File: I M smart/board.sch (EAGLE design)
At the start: 26 parts, among them IC1 TL072P

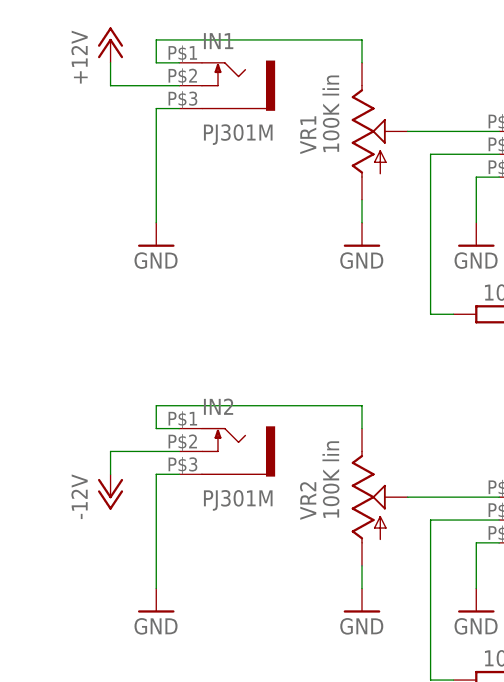
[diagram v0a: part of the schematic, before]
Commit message: Don't connect the power rails directly to output as it shorts the entire case if connected to GND!
Update I M smart to rev0.1. Compatible with panel.
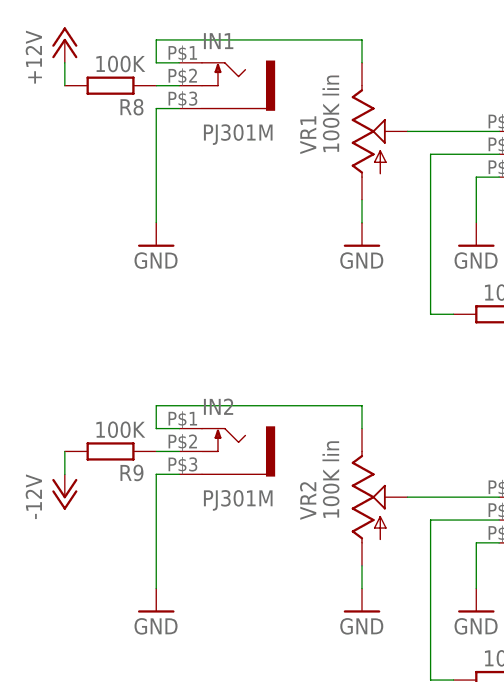
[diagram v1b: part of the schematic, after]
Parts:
- added R8, R9: 100K, rcl:R-EU_0204/5
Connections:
- new net N$11: IN2.3, R9.1
- new net N$12: IN1.3, R8.1
- net +12V: now also R8.2; no longer IN1.3
- net -12V: now also R9.2; no longer IN2.3
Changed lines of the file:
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@@
+<attribute name="OC_FARNELL" value="2329853"/>
+</part>
+<part name="R8" library="rcl" library_urn="urn:adsk.eagle:library:334" deviceset="R-EU_" device="0204/5" package3d_urn="urn:adsk.eagle:package:23488/1" value="100K">
+<spice>
+<pinmapping spiceprefix="R">
+<pinmap gate="G$1" pin="1" pinorder="1"/>
+<pinmap gate="G$1" pin="2" pinorder="2"/>
+</pinmapping>
+</spice>
+<attribute name="MF" value="TE CONNECTIVITY"/>
+<attribute name="MPN" value="LR0204F100K"/>
+<attribute name="OC_FARNELL" value="2329853"/>
+</part>
+<part name="R9" library="rcl" library_urn="urn:adsk.eagle:library:334" deviceset="R-EU_" device="0204/5" package3d_urn="urn:adsk.eagle:package:23488/1" value="100K">
+<spice>
+<pinmapping spiceprefix="R">
+<pinmap gate="G$1" pin="1" pinorder="1"/>
+<pinmap gate="G$1" pin="2" pinorder="2"/>
+</pinmapping>
+</spice>
+<attribute name="MF" value="TE CONNECTIVITY"/>
+<attribute name="MPN" value="LR0204F100K"/>
 <attribute name="OC_FARNELL" value="2329853"/>
 </part>
@@
 <attribute name="MPN" x="35.56" y="99.06" size="1.778" layer="96" display="off"/>
 </instance>
-<instance part="P+1" gate="1" x="7.62" y="149.86" smashed="yes">
-<attribute name="VALUE" x="5.08" y="144.78" size="1.778" layer="96" rot="R90"/>
-</instance>
-<instance part="P-2" gate="1" x="7.62" y="99.06" smashed="yes">
-<attribute name="VALUE" x="5.08" y="96.52" size="1.778" layer="96" rot="R90"/>
+<instance part="P+1" gate="1" x="2.54" y="149.86" smashed="yes">
+<attribute name="VALUE" x="0" y="144.78" size="1.778" layer="96" rot="R90"/>
+</instance>
+<instance part="P-2" gate="1" x="2.54" y="99.06" smashed="yes">
+<attribute name="VALUE" x="0" y="96.52" size="1.778" layer="96" rot="R90"/>
 </instance>
 <instance part="GND1" gate="1" x="12.7" y="127" smashed="yes">
@@
 </instance>
 <instance part="IC1" gate="P" x="73.66" y="27.94" smashed="yes"/>
+<instance part="R8" gate="G$1" x="7.62" y="144.78" smashed="yes" rot="R180">
+<attribute name="NAME" x="11.43" y="143.2814" size="1.778" layer="95" rot="R180"/>
+<attribute name="VALUE" x="11.43" y="148.082" size="1.778" layer="96" rot="R180"/>
+<attribute name="OC_FARNELL" x="7.62" y="144.78" size="1.778" layer="96" display="off"/>
+<attribute name="MF" x="7.62" y="144.78" size="1.778" layer="96" display="off"/>
+<attribute name="MPN" x="7.62" y="144.78" size="1.778" layer="96" display="off"/>
+</instance>
+<instance part="R9" gate="G$1" x="7.62" y="104.14" smashed="yes" rot="R180">
+<attribute name="NAME" x="11.43" y="102.6414" size="1.778" layer="95" rot="R180"/>
+<attribute name="VALUE" x="11.43" y="107.442" size="1.778" layer="96" rot="R180"/>
+<attribute name="OC_FARNELL" x="7.62" y="104.14" size="1.778" layer="96" display="off"/>
+<attribute name="MF" x="7.62" y="104.14" size="1.778" layer="96" display="off"/>
+<attribute name="MPN" x="7.62" y="104.14" size="1.778" layer="96" display="off"/>
+</instance>
 </instances>
 <busses>
@@
 </segment>
 <segment>
-<pinref part="IN1" gate="G$1" pin="3"/>
-<wire x1="15.24" y1="144.78" x2="7.62" y2="144.78" width="0.1524" layer="91"/>
-<wire x1="7.62" y1="144.78" x2="7.62" y2="147.32" width="0.1524" layer="91"/>
+<wire x1="2.54" y1="144.78" x2="2.54" y2="147.32" width="0.1524" layer="91"/>
 <pinref part="P+1" gate="1" pin="+12V"/>
+<pinref part="R8" gate="G$1" pin="2"/>
 </segment>
 </net>
@@
 </segment>
 <segment>
-<pinref part="IN2" gate="G$1" pin="3"/>
-<wire x1="15.24" y1="104.14" x2="7.62" y2="104.14" width="0.1524" layer="91"/>
-<wire x1="7.62" y1="104.14" x2="7.62" y2="101.6" width="0.1524" layer="91"/>
+<wire x1="2.54" y1="104.14" x2="2.54" y2="101.6" width="0.1524" layer="91"/>
 <pinref part="P-2" gate="1" pin="-12V"/>
+<pinref part="R9" gate="G$1" pin="2"/>
 </segment>
 </net>
@@
 </segment>
 </net>
+<net name="N$11" class="0">
+<segment>
+<pinref part="R9" gate="G$1" pin="1"/>
+<pinref part="IN2" gate="G$1" pin="3"/>
+<wire x1="12.7" y1="104.14" x2="15.24" y2="104.14" width="0.1524" layer="91"/>
+</segment>
+</net>
+<net name="N$12" class="0">
+<segment>
+<pinref part="R8" gate="G$1" pin="1"/>
+<pinref part="IN1" gate="G$1" pin="3"/>
+<wire x1="12.7" y1="144.78" x2="15.24" y2="144.78" width="0.1524" layer="91"/>
+</segment>
+</net>
